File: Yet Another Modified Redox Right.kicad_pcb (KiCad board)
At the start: 2 copper layers, 180 x 126 mm, 81 parts, among them J3 AudioJack4, K36 KEYSW, K37 KEYSW, K38 KEYSW, K39 KEYSW, K40 KEYSW, K41 KEYSW, K42 KEYSW, K43 KEYSW, K44 KEYSW, K45 KEYSW, K46 KEYSW, K47 KEYSW, K48 KEYSW, K49 KEYSW, K50 KEYSW, K51 KEYSW, K52 KEYSW, K53 KEYSW, K54 KEYSW, K55 KEYSW, K56 KEYSW, K57 KEYSW, K58 KEYSW, K59 KEYSW, K60 KEYSW, K61 KEYSW, K62 KEYSW, K63 KEYSW, K64 KEYSW, K65 KEYSW, K66 KEYSW, K67 KEYSW, K68 KEYSW, K69 KEYSW, K70 KEYSW, U2 YAAJ_BluePill_Part_Like

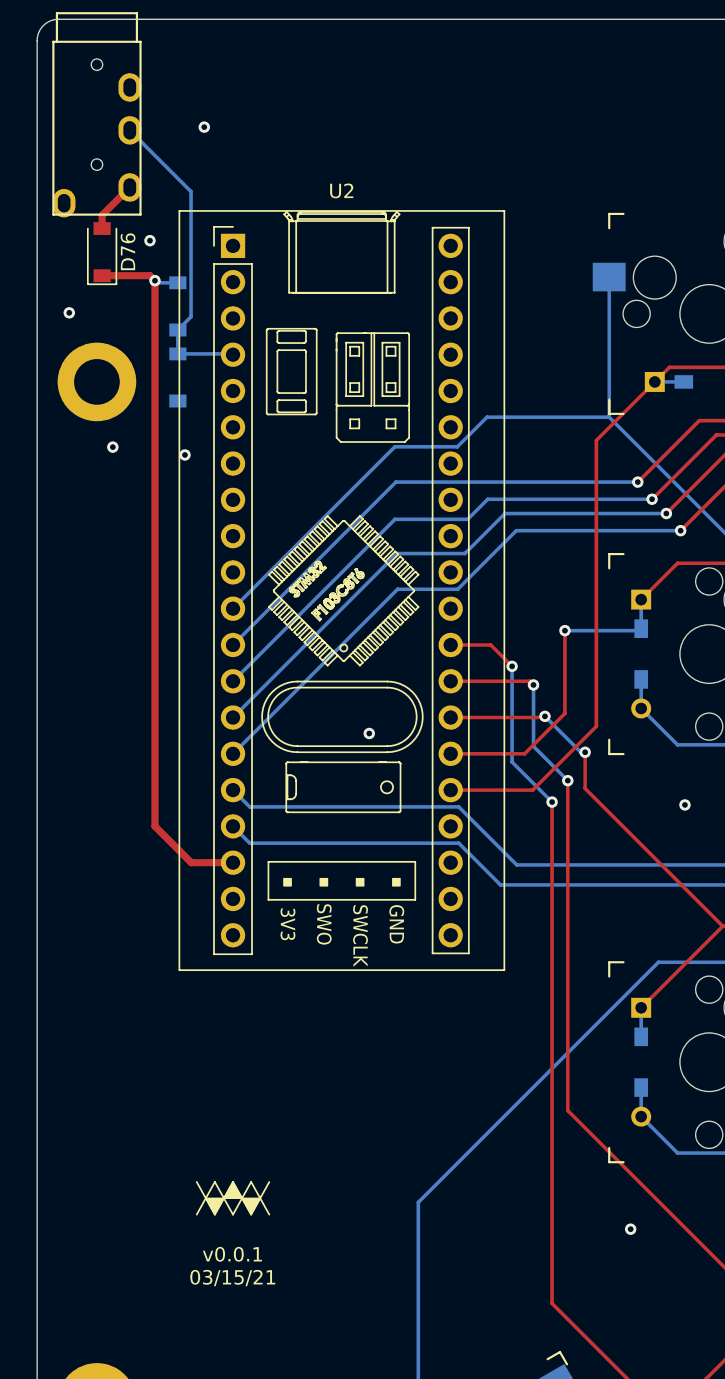
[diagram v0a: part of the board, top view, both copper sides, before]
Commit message: Update to use rp2040 stamp
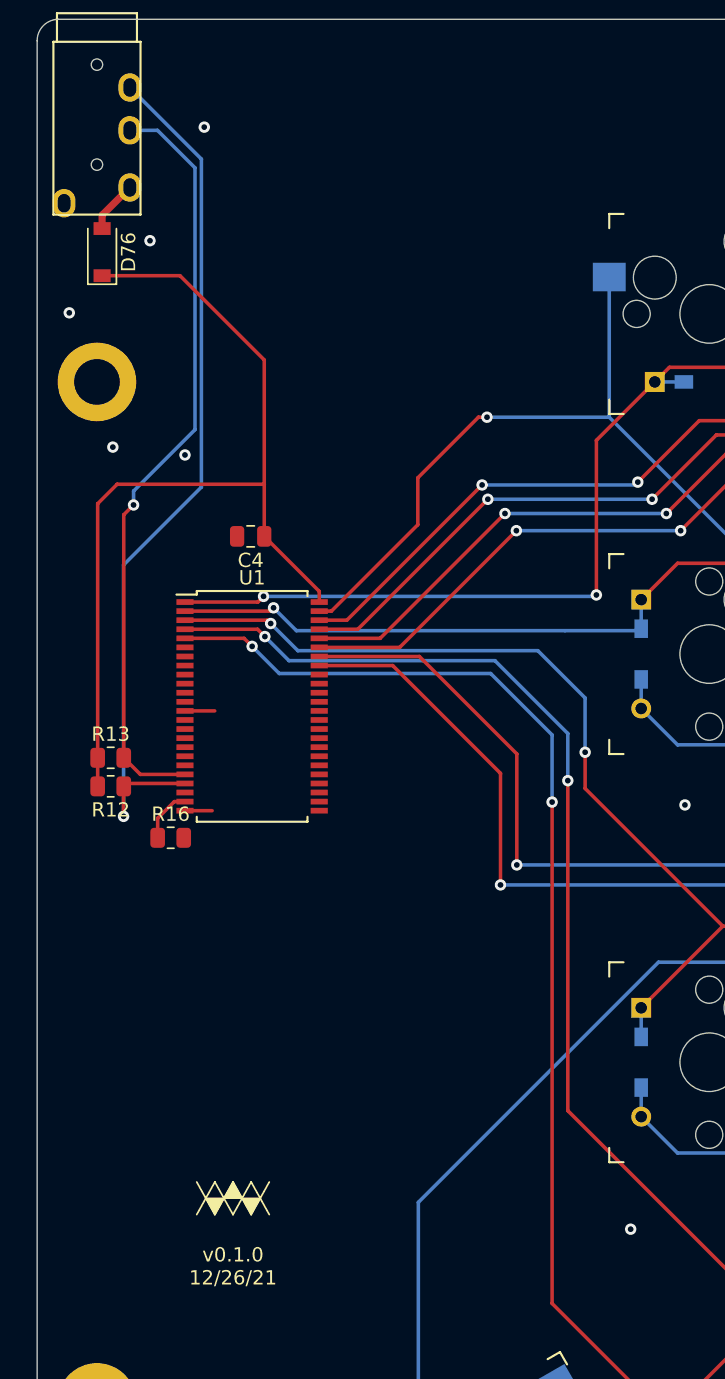
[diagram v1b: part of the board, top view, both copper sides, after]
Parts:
- removed D74, D75: D_Schottky, Diode_SMD:D_SOD-123
- removed U2: YAAJ_BluePill_Part_Like, Footprints:YAAJ_BluePill_1
- added C4: 1uF, Capacitor_SMD:C_0805_2012Metric, F.Cu at (234.6, 63.2)
- added R12: 1kR, Resistor_SMD:R_0805_2012Metric, F.Cu at (224.8, 80.7)
- added R13: 1kR, Resistor_SMD:R_0805_2012Metric, F.Cu at (224.8, 78.7)
- added R16: 100R, Resistor_SMD:R_0805_2012Metric, F.Cu at (229.0, 84.3)
- added U1: CY8C9540A-IOExpander, Package_SO:SSOP-48_7.5x15.9mm_P0.635mm, F.Cu at (234.7, 75.1)
- renumbered REF** to H2, REF** to H3, REF** to H4, REF** to H5
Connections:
- J3 pad R1: /RX -> /SCL_S
- J3 pad R2: (no net) -> /SDA_S
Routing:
- net /SDA_S: track 0.00 -> 61.8 mm, vias 0 -> 1
- net /SCL_S: track 0.00 -> 53.8 mm, vias 0 -> 1
- net /RR3: track 167.5 -> 191.1 mm
- net /RX: track 21.7 -> 0.00 mm
- net /RR4: track 215.7 -> 235.3 mm
- net /RR5: track 232.5 -> 250.1 mm
- net /R+5V: track 50.2 -> 64.4 mm, vias 1 -> 0
- net /RR2: track 162.5 -> 174.9 mm
- net /RC5: track 186.8 -> 177.7 mm, vias 2 -> 3
- net /RC4: track 167.4 -> 159.1 mm, vias 2 -> 3
- net /RR1: track 176.2 -> 184.0 mm, vias 0 -> 2
- net /RC3: track 147.8 -> 140.3 mm, vias 2 -> 3
- net /RC2: track 130.1 -> 123.3 mm, vias 2 -> 3
- net /RC1: track 161.6 -> 157.5 mm, vias 0 -> 1
- net /RGND: track 0.00 -> 3.98 mm, vias 8 -> 7
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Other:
- rule pad_to_mask_clearance: 0.05 -> 0
- board text added: "v0.1.0 12/26/21"
- board text removed: "v0.0.1 03/15/21"
